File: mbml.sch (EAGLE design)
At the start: 44 parts, among them K1 G5SB, K2 68800611622, Q1 2N2222, Q2 IRLZ24LPBF, U1 REG_5V_SWITCHING_SI-8050E, X1 43160-1102, X2 CON-2

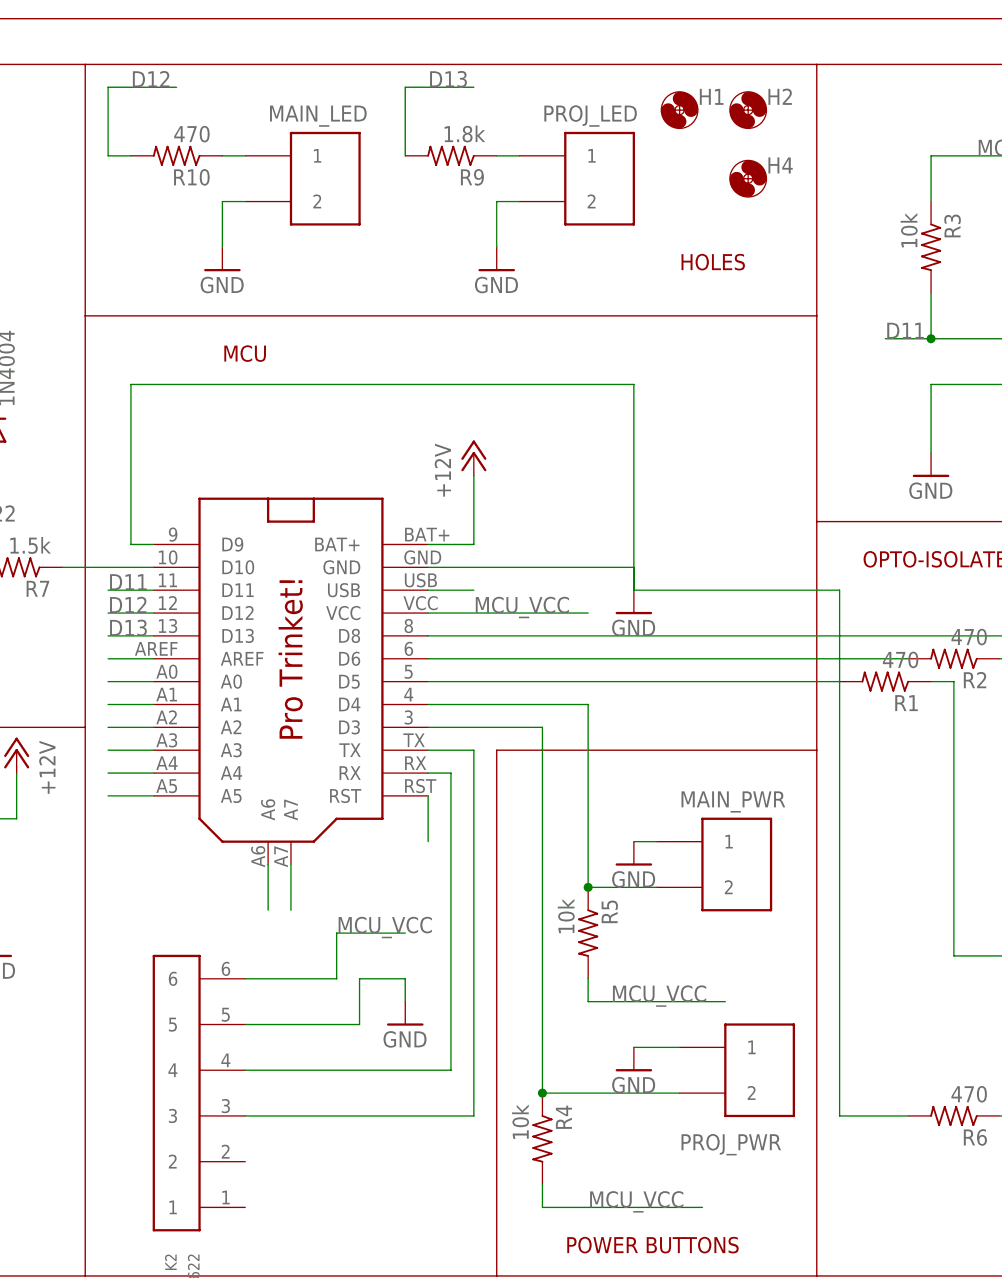
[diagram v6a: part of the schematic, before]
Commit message: Set correct values for button LED current limiting resistors
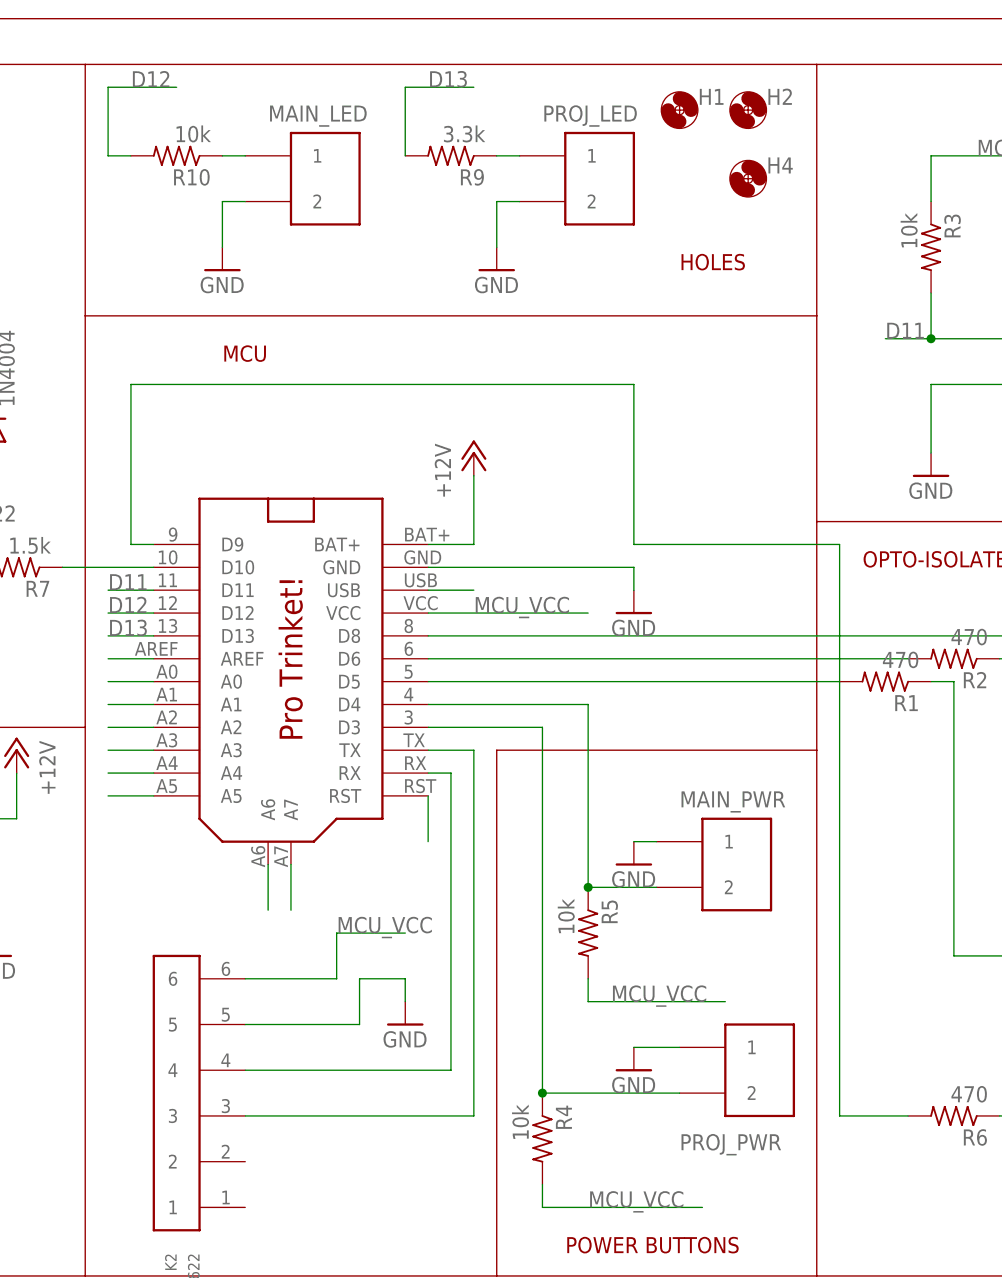
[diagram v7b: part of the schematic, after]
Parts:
- R10: value 470 -> 10k
- R9: value 1.8k -> 3.3k
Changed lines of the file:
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@@
 <part name="GND16" library="supply1" deviceset="GND" device=""/>
 <part name="GND17" library="supply1" deviceset="GND" device=""/>
-<part name="R9" library="resistor" deviceset="R-US_" device="0204/5" value="1.8k"/>
-<part name="R10" library="resistor" deviceset="R-US_" device="0204/5" value="470"/>
+<part name="R9" library="resistor" deviceset="R-US_" device="0204/5" value="3.3k"/>
+<part name="R10" library="resistor" deviceset="R-US_" device="0204/5" value="10k"/>
 <part name="Q2" library="transistor-power" deviceset="PMOSFET_N" device="" value="IRLZ24LPBF"/>
 <part name="R11" library="resistor" deviceset="R-US_" device="0204/5" value="100"/>
@@
 <pinref part="R6" gate="G$1" pin="2"/>
 <wire x1="160.02" y1="96.52" x2="152.4" y2="96.52" width="0.1524" layer="91"/>
-<wire x1="152.4" y1="96.52" x2="152.4" y2="154.94" width="0.1524" layer="91"/>
-<wire x1="152.4" y1="154.94" x2="129.54" y2="154.94" width="0.1524" layer="91"/>
-<wire x1="129.54" y1="154.94" x2="129.54" y2="177.8" width="0.1524" layer="91"/>
+<wire x1="152.4" y1="96.52" x2="152.4" y2="160.02" width="0.1524" layer="91"/>
+<wire x1="152.4" y1="160.02" x2="129.54" y2="160.02" width="0.1524" layer="91"/>
+<wire x1="129.54" y1="160.02" x2="129.54" y2="177.8" width="0.1524" layer="91"/>
 <wire x1="129.54" y1="177.8" x2="73.66" y2="177.8" width="0.1524" layer="91"/>
 <pinref part="U$1" gate="G$1" pin="D9"/>

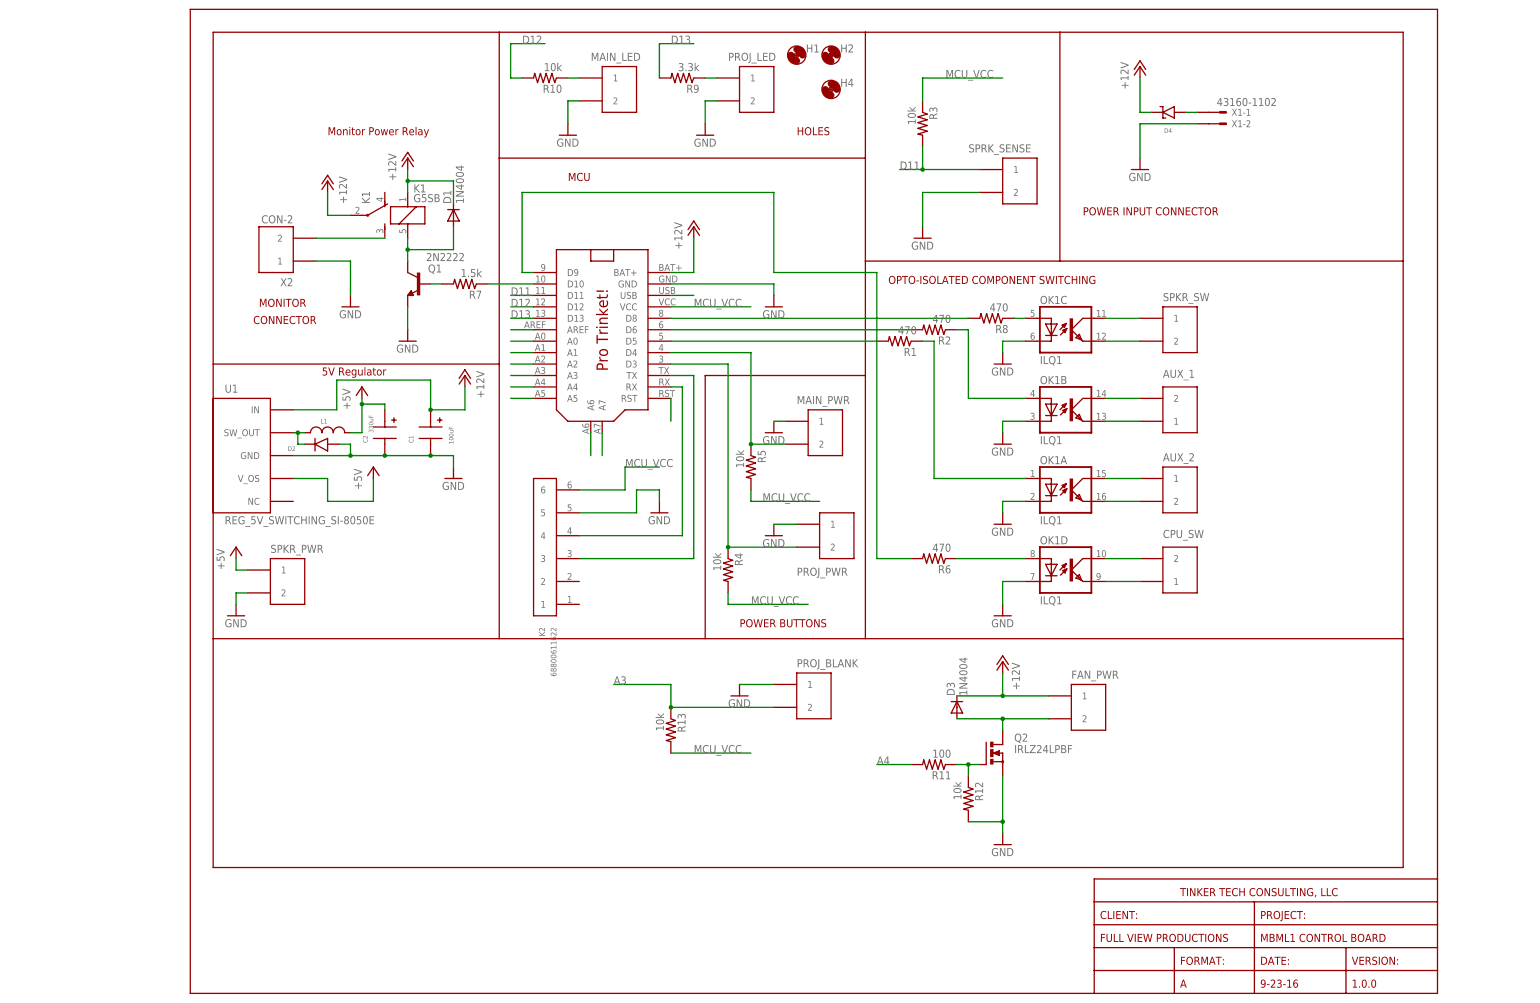
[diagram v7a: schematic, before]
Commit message: MBMLV2.2
Fixed backwards pins on fan MOSFET, added note about switching 5V
regulator to a version that supports a higher current draw.
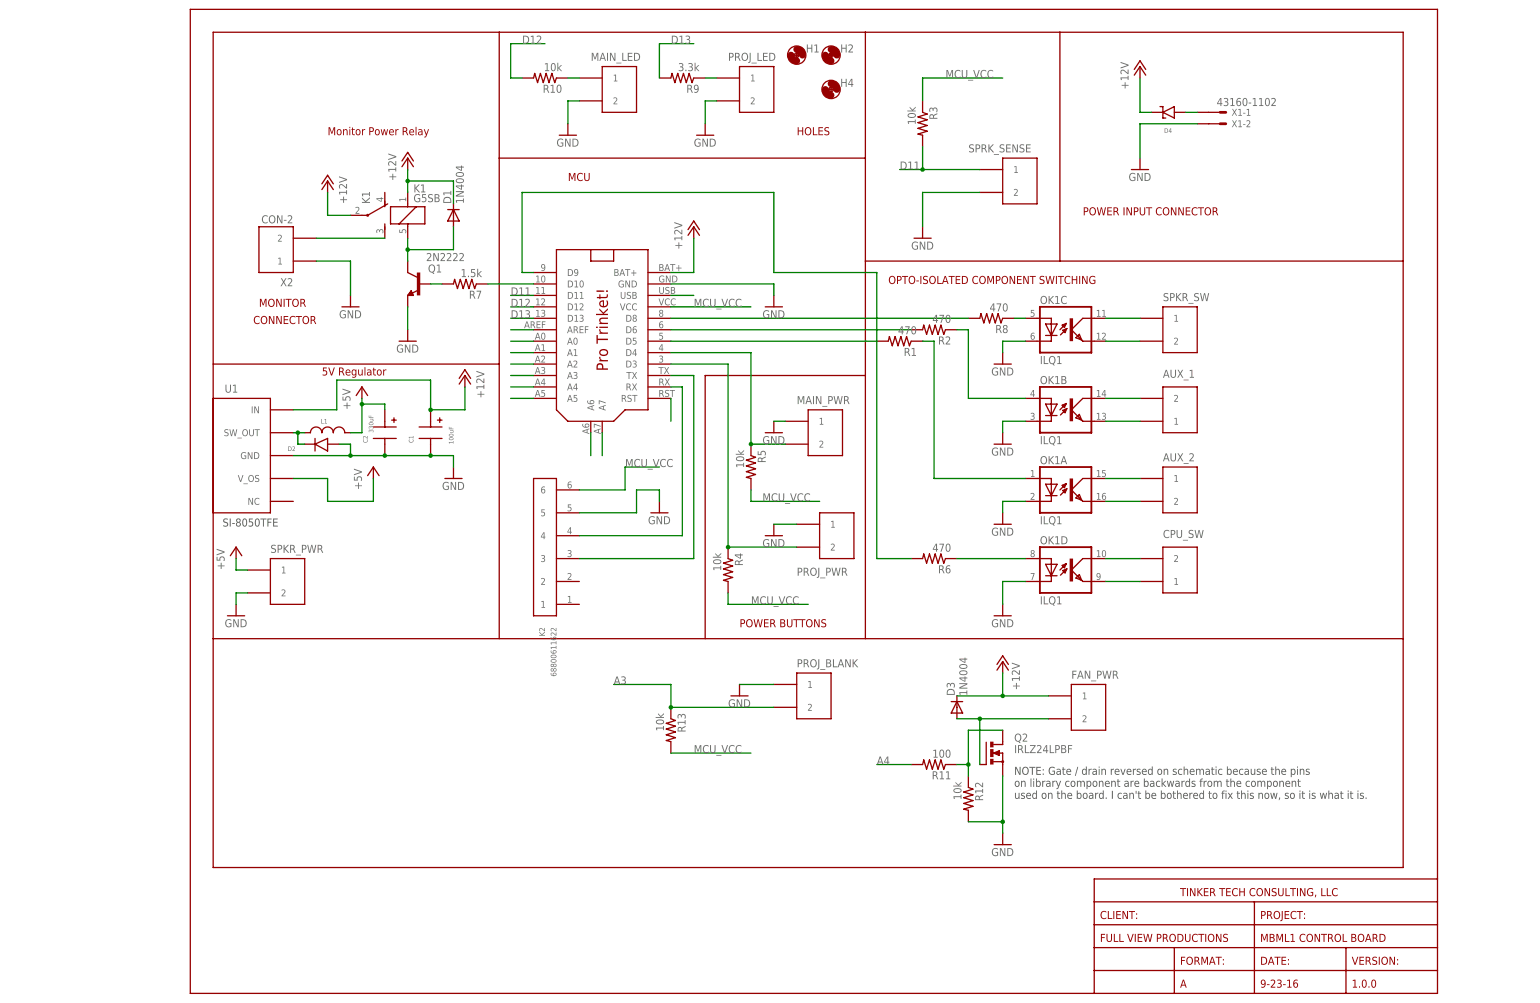
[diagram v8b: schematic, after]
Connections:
- net N$10: now also Q2.D; no longer Q2.G
- net N$9: now also Q2.G; no longer Q2.D
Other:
- note added: "NOTE: Gate / drain reversed on schematic because the pins on library component are backwards from the component used on the board. I can't be bothered to fix this now, so it is what it is."
- note added: "SI-8050TFE"
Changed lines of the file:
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@@
 <?xml version="1.0" encoding="utf-8"?>
 <!DOCTYPE eagle SYSTEM "eagle.dtd">
-<eagle version="7.6.0">
+<eagle version="8.2.2">
 <drawing>
 <settings>
@@
 <wire x1="193.04" y1="162.56" x2="193.04" y2="213.36" width="0.1524" layer="94"/>
 <wire x1="5.08" y1="78.74" x2="269.24" y2="78.74" width="0.1524" layer="94"/>
+<text x="19.558" y="105.41" size="1.778" layer="97" rot="R180">SI-8050TFE</text>
+<text x="182.88" y="43.18" size="1.778" layer="97">NOTE: Gate / drain reversed on schematic because the pins
+on library component are backwards from the component
+used on the board. I can't be bothered to fix this now, so it is what it is.</text>
 </plain>
 <instances>
@@
 <instance part="GND10" gate="1" x="180.34" y="33.02"/>
 <instance part="GND11" gate="1" x="104.14" y="106.68"/>
-<instance part="U1" gate="G$1" x="12.7" y="119.38"/>
+<instance part="U1" gate="G$1" x="12.7" y="119.38" smashed="yes">
+<attribute name="NAME" x="7.62" y="133.35" size="1.778" layer="95"/>
+</instance>
 <instance part="L1" gate="G$1" x="30.48" y="124.46" smashed="yes">
 <attribute name="NAME" x="28.956" y="126.492" size="1.016" layer="95"/>
@@
 <segment>
 <pinref part="FAN_PWR" gate="G$1" pin="2"/>
-<pinref part="Q2" gate="G$1" pin="D"/>
-<wire x1="190.5" y1="60.96" x2="180.34" y2="60.96" width="0.1524" layer="91"/>
-<wire x1="180.34" y1="60.96" x2="180.34" y2="58.42" width="0.1524" layer="91"/>
 <pinref part="D3" gate="1" pin="A"/>
-<wire x1="170.18" y1="60.96" x2="180.34" y2="60.96" width="0.1524" layer="91"/>
-<junction x="180.34" y="60.96"/>
+<wire x1="170.18" y1="60.96" x2="175.26" y2="60.96" width="0.1524" layer="91"/>
+<pinref part="Q2" gate="G$1" pin="G"/>
+<wire x1="175.26" y1="60.96" x2="190.5" y2="60.96" width="0.1524" layer="91"/>
+<wire x1="175.26" y1="50.8" x2="175.26" y2="60.96" width="0.1524" layer="91"/>
+<junction x="175.26" y="60.96"/>
 </segment>
 </net>
@@
 <segment>
 <pinref part="R11" gate="G$1" pin="1"/>
-<pinref part="Q2" gate="G$1" pin="G"/>
 <wire x1="170.18" y1="50.8" x2="172.72" y2="50.8" width="0.1524" layer="91"/>
 <pinref part="R12" gate="G$1" pin="1"/>
-<wire x1="172.72" y1="50.8" x2="175.26" y2="50.8" width="0.1524" layer="91"/>
 <wire x1="172.72" y1="48.26" x2="172.72" y2="50.8" width="0.1524" layer="91"/>
+<pinref part="Q2" gate="G$1" pin="D"/>
+<wire x1="180.34" y1="58.42" x2="172.72" y2="58.42" width="0.1524" layer="91"/>
+<wire x1="172.72" y1="58.42" x2="172.72" y2="50.8" width="0.1524" layer="91"/>
 <junction x="172.72" y="50.8"/>
 </segment>
@@
 </schematic>
 </drawing>
+<compatibility>
+<note version="6.3" minversion="6.2.2" severity="warning">
+Since Version 6.2.2 text objects can contain more than one line,
+which will not be processed correctly with this version.
+</note>
+</compatibility>
 </eagle>
